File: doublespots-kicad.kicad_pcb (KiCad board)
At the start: 2 copper layers, 15 x 6.3 mm, 9 parts

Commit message: needed a via and not so nice routing... but no more errors
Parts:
- moved DO 0.15 mm to (0.00, 1.80)
- moved GND1 0.11 mm to (-6.15, 1.42)
- moved VDD2 0.11 mm to (6.15, -1.42)
- moved GND2 0.10 mm to (6.15, 1.42)
- moved DI 0.10 mm to (0.00, -1.80)
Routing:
- net /GND: track 14.1 -> 19.2 mm
- net /VDD: track 14.1 -> 19.1 mm
- net /DInt: track 9.65 -> 9.91 mm, vias 0 -> 1
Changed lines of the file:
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@@
 	(footprint "MyLibrary:TestPoint_Pad_2.4x1.6mm"
 		(layer "F.Cu")
-		(at 6.25 -1.46 -90)
+		(at 6.15 -1.42 -90)
 		(descr "SMD rectangular pad as test Point, square 1.5mm side length")
 		(tags "test point SMD pad rectangle square")
@@
 	(footprint "MyLibrary:TestPoint_Pad_2.4x1.6mm"
 		(layer "F.Cu")
-		(at 6.25 1.44 -90)
+		(at 6.15 1.42 -90)
 		(descr "SMD rectangular pad as test Point, square 1.5mm side length")
 		(tags "test point SMD pad rectangle square")
@@
 	(footprint "MyLibrary:TestPoint_Pad_2.4x1.6mm"
 		(layer "F.Cu")
-		(at -0.01 -1.9)
+		(at 0 -1.8)
 		(descr "SMD rectangular pad as test Point, square 1.5mm side length")
 		(tags "test point SMD pad rectangle square")
@@
 	(footprint "MyLibrary:TestPoint_Pad_2.4x1.6mm"
 		(layer "F.Cu")
-		(at 0.06 1.94)
+		(at 0 1.8)
 		(descr "SMD rectangular pad as test Point, square 1.5mm side length")
 		(tags "test point SMD pad rectangle square")
@@
 	(footprint "MyLibrary:TestPoint_Pad_2.4x1.6mm"
 		(layer "F.Cu")
-		(at -6.16 1.53 90)
+		(at -6.15 1.42 90)
 		(descr "SMD rectangular pad as test Point, square 1.5mm side length")
 		(tags "test point SMD pad rectangle square")
@@
 	(footprint "MyLibrary:TestPoint_Pad_2.4x1.6mm"
 		(layer "F.Cu")
-		(at -6.15 -1.39 90)
+		(at -6.15 -1.42 90)
 		(descr "SMD rectangular pad as test Point, square 1.5mm side length")
 		(tags "test point SMD pad rectangle square")
@@
 		)
 		(pad "1" smd rect
-			(at 0 0 90)
+			(at 0.01 0 90)
 			(size 2.4 1.6)
 			(layers "F.Cu" "F.Mask")
@@
 	)
 	(segment
-		(start -0.775 0)
-		(end -0.775 0.834)
-		(width 0.2)
-		(layer "F.Cu")
-		(net 1)
-	)
-	(segment
 		(start -5.295 0.665)
 		(end -4 0.665)
@@
 	)
 	(segment
-		(start -0.78 0.839)
-		(end 3.826 0.839)
+		(start -4 0.665)
+		(end -3.655 0.665)
+		(width 0.2)
+		(layer "F.Cu")
+		(net 1)
+	)
+	(segment
+		(start -3.655 0.665)
+		(end -2.12 -0.87)
 		(width 0.2)
 		(layer "F.Cu")
@@
 	)
 	(segment
-		(start -0.775 0.834)
-		(end -0.78 0.839)
-		(width 0.2)
-		(layer "F.Cu")
-		(net 1)
-	)
-	(segment
-		(start -3.826 0.839)
-		(end -0.78 0.839)
+		(start -2.12 -0.87)
+		(end -1.645 -0.87)
 		(width 0.2)
 		(layer "F.Cu")
@@
 	)
 	(segment
-		(start 3.826 0.839)
+		(start -1.645 -0.87)
+		(end -0.775 0)
+		(width 0.2)
+		(layer "F.Cu")
+		(net 1)
+	)
+	(segment
+		(start 1.39 2.37)
+		(end 3.095 0.665)
+		(width 0.2)
+		(layer "B.Cu")
+		(net 1)
+	)
+	(segment
+		(start -4 0.665)
+		(end -2.945 0.665)
+		(width 0.2)
+		(layer "B.Cu")
+		(net 1)
+	)
+	(segment
+		(start 3.095 0.665)
 		(end 4 0.665)
 		(width 0.2)
-		(layer "F.Cu")
+		(layer "B.Cu")
+		(net 1)
+	)
+	(segment
+		(start -2.945 0.665)
+		(end -1.24 2.37)
+		(width 0.2)
+		(layer "B.Cu")
+		(net 1)
+	)
+	(segment
+		(start -1.24 2.37)
+		(end 1.39 2.37)
+		(width 0.2)
+		(layer "B.Cu")
+		(net 1)
+	)
+	(segment
+		(start 3.865 0.53)
+		(end 4 0.665)
+		(width 0.2)
+		(layer "B.Cu")
 		(net 1)
 	)
@@
 	)
 	(segment
-		(start 0.775 0)
-		(end 0.775 -0.771)
-		(width 0.2)
-		(layer "F.Cu")
-		(net 2)
-	)
-	(segment
 		(start -6.3 -1.46)
 		(end -5.505 -0.665)
@@
 	)
 	(segment
-		(start 0.775 -0.771)
-		(end 0.77 -0.776)
-		(width 0.2)
-		(layer "F.Cu")
-		(net 2)
-	)
-	(segment
-		(start 0.77 -0.776)
-		(end 3.889 -0.776)
-		(width 0.2)
-		(layer "F.Cu")
-		(net 2)
-	)
-	(segment
-		(start -3.889 -0.776)
-		(end 0.77 -0.776)
+		(start 1.75 0)
+		(end 2.415 -0.665)
+		(width 0.2)
+		(layer "F.Cu")
+		(net 2)
+	)
+	(segment
+		(start 0.775 0)
+		(end 1.75 0)
 		(width 0.2)
 		(layer "F.Cu")
@@
 	)
 	(segment
-		(start -4 -0.665)
-		(end -3.889 -0.776)
+		(start 2.415 -0.665)
+		(end 4 -0.665)
 		(width 0.2)
 		(layer "F.Cu")
@@
 	)
 	(segment
+		(start -3.521 -0.186)
+		(end -3.347504 -0.186)
+		(width 0.2)
+		(layer "B.Cu")
+		(net 2)
+	)
+	(segment
+		(start -2.897504 0.264)
+		(end -2.7789 0.264)
+		(width 0.2)
+		(layer "B.Cu")
+		(net 2)
+	)
+	(segment
+		(start 1.2239 1.969)
+		(end 2.849 0.3439)
+		(width 0.2)
+		(layer "B.Cu")
+		(net 2)
+	)
+	(segment
+		(start -2.7789 0.264)
+		(end -1.0739 1.969)
+		(width 0.2)
+		(layer "B.Cu")
+		(net 2)
+	)
+	(segment
+		(start -3.347504 -0.186)
+		(end -2.897504 0.264)
+		(width 0.2)
+		(layer "B.Cu")
+		(net 2)
+	)
+	(segment
+		(start 2.849 0.312504)
+		(end 3.347504 -0.186)
+		(width 0.2)
+		(layer "B.Cu")
+		(net 2)
+	)
+	(segment
+		(start 2.849 0.3439)
+		(end 2.849 0.312504)
+		(width 0.2)
+		(layer "B.Cu")
+		(net 2)
+	)
+	(segment
+		(start 3.521 -0.186)
+		(end 4 -0.665)
+		(width 0.2)
+		(layer "B.Cu")
+		(net 2)
+	)
+	(segment
+		(start 3.347504 -0.186)
+		(end 3.521 -0.186)
+		(width 0.2)
+		(layer "B.Cu")
+		(net 2)
+	)
+	(segment
+		(start -1.0739 1.969)
+		(end 1.2239 1.969)
+		(width 0.2)
+		(layer "B.Cu")
+		(net 2)
+	)
+	(segment
+		(start -4 -0.665)
+		(end -3.521 -0.186)
+		(width 0.2)
+		(layer "B.Cu")
+		(net 2)
+	)
+	(segment
 		(start -4 -1.995)
 		(end -0.105 -1.995)
@@
 	)
 	(segment
-		(start 0.29 -1.995)
-		(end 4 -1.995)
-		(width 0.2)
-		(layer "B.Cu")
-		(net 4)
-	)
-	(segment
-		(start -3.7 1.995)
-		(end 0.29 -1.995)
-		(width 0.2)
-		(layer "B.Cu")
+		(start -1.8825 0.1775)
+		(end -1.8825 -0.25897)
+		(width 0.2)
+		(layer "F.Cu")
 		(net 4)
 	)
@@
 		(end -3.7 1.995)
 		(width 0.2)
-		(layer "B.Cu")
+		(layer "F.Cu")
+		(net 4)
+	)
+	(segment
+		(start -3.7 1.995)
+		(end -1.8825 0.1775)
+		(width 0.2)
+		(layer "F.Cu")
+		(net 4)
+	)
+	(via
+		(at -1.8825 -0.25897)
+		(size 0.6)
+		(drill 0.3)
+		(layers "F.Cu" "B.Cu")
+		(free yes)
+		(net 4)
+	)
+	(segment
+		(start -1.8825 -0.25897)
+		(end -0.14647 -1.995)
+		(width 0.2)
+		(layer "B.Cu")
+		(net 4)
+	)
+	(segment
+		(start -0.14647 -1.995)
+		(end 4 -1.995)
+		(width 0.2)
+		(layer "B.Cu")

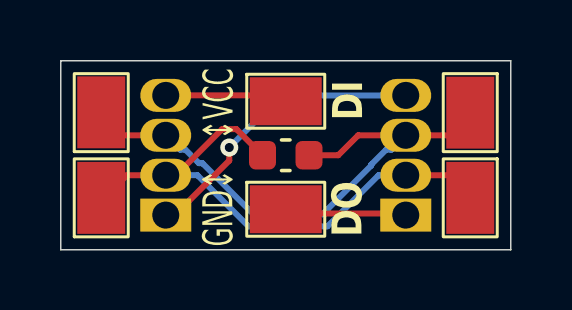
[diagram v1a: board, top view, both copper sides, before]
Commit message: Update PCB with connectors and ground plane
This change also adds a ground plane and reworks some routing.

Signed-off-by: Markus Hutzler <markus.hutzler@me.com>
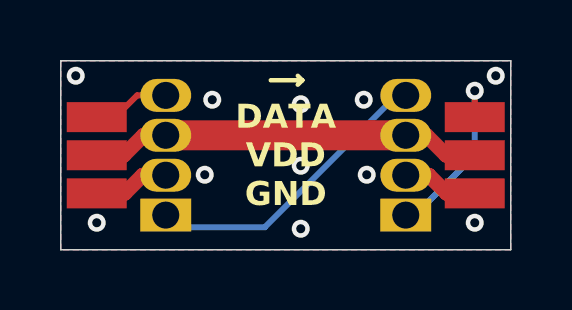
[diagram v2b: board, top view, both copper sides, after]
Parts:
- removed C1: 100nf, Capacitor_SMD:C_0603_1608Metric
- removed DI: DI, MyLibrary:TestPoint_Pad_2.4x1.6mm
- removed DO: DO, MyLibrary:TestPoint_Pad_2.4x1.6mm
- removed GND1, GND2: GND, MyLibrary:TestPoint_Pad_2.4x1.6mm
- removed VDD1, VDD2: VDD, MyLibrary:TestPoint_Pad_2.4x1.6mm
- added J1: Conn_01x03_Pin, MyLibrary:con_1x03_solder, F.Cu at (-6.30, 0.00)
- added J2: Conn_01x03_Pin, MyLibrary:con_1x03_solder, F.Cu at (6.30, 0.00)
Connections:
- net /GND renamed GND
- net /VDD renamed VDD
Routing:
- net GND: track 19.2 -> 5.12 mm, vias 0 -> 11
- net /DO: track 3.96 -> 9.85 mm, vias 0 -> 1
- net VDD: track 19.1 -> 13.7 mm
- net /DI: track 4.03 -> 3.18 mm
- net /DInt: track 9.91 -> 9.99 mm, vias 1 -> 0
- added copper zone on B.Cu, net GND
- added copper zone on F.Cu, net GND
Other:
- board text added: "DATA VDD GND"
- board text removed: "GND↕"
- board text removed: "↕VCC"
